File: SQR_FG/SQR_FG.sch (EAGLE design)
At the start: 24 parts, among them IC1 MEGA328P, IC2 NJM7032, Q1 16MHz, SW1 EC12E_SW

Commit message: SQR_FG Bypass by C
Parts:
- removed C7: (no value), rcl:C-EU025-024X044
- removed R4, R5: (no value), rcl:R-EU_0207/7
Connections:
- removed net N$14: C6.2, IC2A.+IN, R4.2
- removed net N$4: C7.1, R4.1, R5.2
- net N$15: now also C6.2, IC2A.+IN; no longer R5.1
- net N$16: no longer C7.2
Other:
- moved on the sheet: C5, C6, IC2A, JP2, R6
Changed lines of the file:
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@@
 <part name="JP2" library="pinhead" deviceset="PINHD-1X2" device=""/>
 <part name="R3" library="rcl" deviceset="R-EU_" device="0207/7" value="33k"/>
-<part name="R4" library="rcl" deviceset="R-EU_" device="0207/7"/>
-<part name="R5" library="rcl" deviceset="R-EU_" device="0207/7"/>
 <part name="C6" library="rcl" deviceset="C-EU" device="025-024X044"/>
-<part name="C7" library="rcl" deviceset="C-EU" device="025-024X044"/>
 <part name="GND6" library="supply1" deviceset="GND" device=""/>
 </parts>
@@
 <instance part="SW1" gate="G$2" x="132.08" y="73.66"/>
 <instance part="GND4" gate="1" x="139.7" y="63.5"/>
-<instance part="P+3" gate="1" x="238.76" y="114.3"/>
-<instance part="GND7" gate="1" x="238.76" y="83.82"/>
-<instance part="IC2" gate="A" x="238.76" y="93.98"/>
+<instance part="P+3" gate="1" x="220.98" y="114.3"/>
+<instance part="GND7" gate="1" x="220.98" y="83.82"/>
+<instance part="IC2" gate="A" x="220.98" y="93.98"/>
 <instance part="IC2" gate="B" x="162.56" y="27.94"/>
-<instance part="IC2" gate="P" x="238.76" y="93.98"/>
-<instance part="R6" gate="G$1" x="259.08" y="93.98"/>
+<instance part="IC2" gate="P" x="220.98" y="93.98"/>
+<instance part="R6" gate="G$1" x="241.3" y="93.98"/>
 <instance part="R7" gate="G$1" x="139.7" y="38.1" rot="R90"/>
 <instance part="R8" gate="G$1" x="139.7" y="22.86" rot="R90"/>
@@
 <instance part="T2" gate="A" x="165.1" y="78.74"/>
 <instance part="GND10" gate="1" x="165.1" y="71.12"/>
-<instance part="C5" gate="G$1" x="243.84" y="104.14" rot="R90"/>
-<instance part="GND5" gate="1" x="254" y="104.14" rot="R90"/>
-<instance part="JP2" gate="G$1" x="274.32" y="91.44"/>
+<instance part="C5" gate="G$1" x="226.06" y="104.14" rot="R90"/>
+<instance part="GND5" gate="1" x="236.22" y="104.14" rot="R90"/>
+<instance part="JP2" gate="G$1" x="256.54" y="91.44"/>
 <instance part="R3" gate="G$1" x="182.88" y="109.22" rot="R90"/>
-<instance part="R4" gate="G$1" x="215.9" y="96.52"/>
-<instance part="R5" gate="G$1" x="200.66" y="96.52"/>
-<instance part="C6" gate="G$1" x="226.06" y="104.14"/>
-<instance part="C7" gate="G$1" x="218.44" y="76.2" rot="R90"/>
-<instance part="GND6" gate="1" x="215.9" y="106.68"/>
+<instance part="C6" gate="G$1" x="208.28" y="104.14"/>
+<instance part="GND6" gate="1" x="198.12" y="106.68"/>
 </instances>
 <busses>
@@
 <pinref part="C5" gate="G$1" pin="2"/>
 <pinref part="GND5" gate="1" pin="GND"/>
-<wire x1="251.46" y1="104.14" x2="248.92" y2="104.14" width="0.1524" layer="91"/>
+<wire x1="233.68" y1="104.14" x2="231.14" y2="104.14" width="0.1524" layer="91"/>
 </segment>
 <segment>
 <pinref part="C6" gate="G$1" pin="1"/>
-<wire x1="226.06" y1="106.68" x2="226.06" y2="111.76" width="0.1524" layer="91"/>
-<wire x1="226.06" y1="111.76" x2="215.9" y2="111.76" width="0.1524" layer="91"/>
+<wire x1="208.28" y1="106.68" x2="208.28" y2="111.76" width="0.1524" layer="91"/>
+<wire x1="208.28" y1="111.76" x2="198.12" y2="111.76" width="0.1524" layer="91"/>
 <pinref part="GND6" gate="1" pin="GND"/>
-<wire x1="215.9" y1="111.76" x2="215.9" y2="109.22" width="0.1524" layer="91"/>
+<wire x1="198.12" y1="111.76" x2="198.12" y2="109.22" width="0.1524" layer="91"/>
 </segment>
 </net>
@@
 <segment>
 <pinref part="IC2" gate="P" pin="V+"/>
-<wire x1="238.76" y1="101.6" x2="238.76" y2="104.14" width="0.1524" layer="91"/>
+<wire x1="220.98" y1="101.6" x2="220.98" y2="104.14" width="0.1524" layer="91"/>
 <pinref part="P+3" gate="1" pin="+5V"/>
 <pinref part="C5" gate="G$1" pin="1"/>
-<wire x1="238.76" y1="104.14" x2="238.76" y2="111.76" width="0.1524" layer="91"/>
-<wire x1="241.3" y1="104.14" x2="238.76" y2="104.14" width="0.1524" layer="91"/>
-<junction x="238.76" y="104.14"/>
+<wire x1="220.98" y1="104.14" x2="220.98" y2="111.76" width="0.1524" layer="91"/>
+<wire x1="223.52" y1="104.14" x2="220.98" y2="104.14" width="0.1524" layer="91"/>
+<junction x="220.98" y="104.14"/>
 </segment>
 </net>
@@
 <net name="N$16" class="0">
 <segment>
-<wire x1="231.14" y1="91.44" x2="228.6" y2="91.44" width="0.1524" layer="91"/>
-<wire x1="228.6" y1="91.44" x2="228.6" y2="76.2" width="0.1524" layer="91"/>
-<wire x1="228.6" y1="76.2" x2="251.46" y2="76.2" width="0.1524" layer="91"/>
-<wire x1="251.46" y1="76.2" x2="251.46" y2="93.98" width="0.1524" layer="91"/>
-<wire x1="251.46" y1="93.98" x2="246.38" y2="93.98" width="0.1524" layer="91"/>
+<wire x1="213.36" y1="91.44" x2="208.28" y2="91.44" width="0.1524" layer="91"/>
+<wire x1="208.28" y1="91.44" x2="208.28" y2="76.2" width="0.1524" layer="91"/>
+<wire x1="208.28" y1="76.2" x2="233.68" y2="76.2" width="0.1524" layer="91"/>
+<wire x1="233.68" y1="76.2" x2="233.68" y2="93.98" width="0.1524" layer="91"/>
+<wire x1="233.68" y1="93.98" x2="228.6" y2="93.98" width="0.1524" layer="91"/>
 <pinref part="IC2" gate="A" pin="-IN"/>
 <pinref part="IC2" gate="A" pin="OUT"/>
 <pinref part="R6" gate="G$1" pin="1"/>
-<wire x1="254" y1="93.98" x2="251.46" y2="93.98" width="0.1524" layer="91"/>
-<junction x="251.46" y="93.98"/>
-<pinref part="C7" gate="G$1" pin="2"/>
-<wire x1="223.52" y1="76.2" x2="228.6" y2="76.2" width="0.1524" layer="91"/>
-<junction x="228.6" y="76.2"/>
+<wire x1="236.22" y1="93.98" x2="233.68" y2="93.98" width="0.1524" layer="91"/>
+<junction x="233.68" y="93.98"/>
 </segment>
 </net>
@@
 <segment>
 <pinref part="R6" gate="G$1" pin="2"/>
-<wire x1="264.16" y1="93.98" x2="271.78" y2="93.98" width="0.1524" layer="91"/>
+<wire x1="246.38" y1="93.98" x2="254" y2="93.98" width="0.1524" layer="91"/>
 <pinref part="JP2" gate="G$1" pin="1"/>
 </segment>
@@
 <wire x1="182.88" y1="86.36" x2="198.12" y2="86.36" width="0.1524" layer="91"/>
 <wire x1="198.12" y1="86.36" x2="198.12" y2="68.58" width="0.1524" layer="91"/>
-<wire x1="198.12" y1="68.58" x2="269.24" y2="68.58" width="0.1524" layer="91"/>
-<wire x1="269.24" y1="68.58" x2="269.24" y2="91.44" width="0.1524" layer="91"/>
+<wire x1="198.12" y1="68.58" x2="251.46" y2="68.58" width="0.1524" layer="91"/>
+<wire x1="251.46" y1="68.58" x2="251.46" y2="91.44" width="0.1524" layer="91"/>
 <pinref part="JP2" gate="G$1" pin="2"/>
-<wire x1="271.78" y1="91.44" x2="269.24" y2="91.44" width="0.1524" layer="91"/>
+<wire x1="254" y1="91.44" x2="251.46" y2="91.44" width="0.1524" layer="91"/>
 </segment>
 </net>
@@
 </segment>
 </net>
-<net name="N$4" class="0">
-<segment>
-<pinref part="R5" gate="G$1" pin="2"/>
-<pinref part="R4" gate="G$1" pin="1"/>
-<wire x1="205.74" y1="96.52" x2="208.28" y2="96.52" width="0.1524" layer="91"/>
-<wire x1="208.28" y1="96.52" x2="210.82" y2="96.52" width="0.1524" layer="91"/>
-<wire x1="218.44" y1="76.2" x2="215.9" y2="76.2" width="0.1524" layer="91"/>
-<wire x1="215.9" y1="76.2" x2="208.28" y2="76.2" width="0.1524" layer="91"/>
-<wire x1="208.28" y1="76.2" x2="208.28" y2="96.52" width="0.1524" layer="91"/>
+<net name="N$15" class="0">
+<segment>
+<wire x1="187.96" y1="96.52" x2="208.28" y2="96.52" width="0.1524" layer="91"/>
+<pinref part="IC2" gate="A" pin="+IN"/>
+<pinref part="C6" gate="G$1" pin="2"/>
+<wire x1="208.28" y1="96.52" x2="213.36" y2="96.52" width="0.1524" layer="91"/>
+<wire x1="208.28" y1="99.06" x2="208.28" y2="96.52" width="0.1524" layer="91"/>
 <junction x="208.28" y="96.52"/>
-<pinref part="C7" gate="G$1" pin="1"/>
-<junction x="215.9" y="76.2"/>
-</segment>
-</net>
-<net name="N$14" class="0">
-<segment>
-<pinref part="R4" gate="G$1" pin="2"/>
-<pinref part="IC2" gate="A" pin="+IN"/>
-<wire x1="220.98" y1="96.52" x2="226.06" y2="96.52" width="0.1524" layer="91"/>
-<pinref part="C6" gate="G$1" pin="2"/>
-<wire x1="226.06" y1="96.52" x2="231.14" y2="96.52" width="0.1524" layer="91"/>
-<wire x1="226.06" y1="99.06" x2="226.06" y2="96.52" width="0.1524" layer="91"/>
-<junction x="226.06" y="96.52"/>
-</segment>
-</net>
-<net name="N$15" class="0">
-<segment>
-<pinref part="R5" gate="G$1" pin="1"/>
-<wire x1="195.58" y1="96.52" x2="187.96" y2="96.52" width="0.1524" layer="91"/>
-</segment>
-</net>
+</segment>
+</net>

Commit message: SQR_FG.sch changed
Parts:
- added C7: (no value), rcl:CPOL-EUE2.5-5
- added R4: 22k, rcl:R-EU_0207/7
- added R5: 12k, rcl:R-EU_0207/7
- C3: value 0.1uF -> (none); device rcl:C-EU025-024X044 -> rcl:CPOL-EUE2.5-5
- JP2: value (none) -> OUT
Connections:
- net N$10 renamed RE_SW
- net N$12 renamed SW_GND
- net N$13 renamed SW_VGND
- net N$5 renamed RE_A
- net N$7 renamed RE_B
- new net AGND: C5.2, C6.1, C7.-, IC2P.V-, R8.1, T2.S
- new net N$4: IC1.PD7(AIN1), R4.1
- net +5V: now also C3.+; no longer C3.1
- net GND: now also R5.2; no longer C3.2, C5.2, C6.1, IC2P.V-, R8.1, T2.S
- net N$17: now also C3.-, C7.+
- net RST: now also R4.2, R5.1; no longer IC1.PD7(AIN1)
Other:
- moved on the sheet: JP1, R3, R7, R8

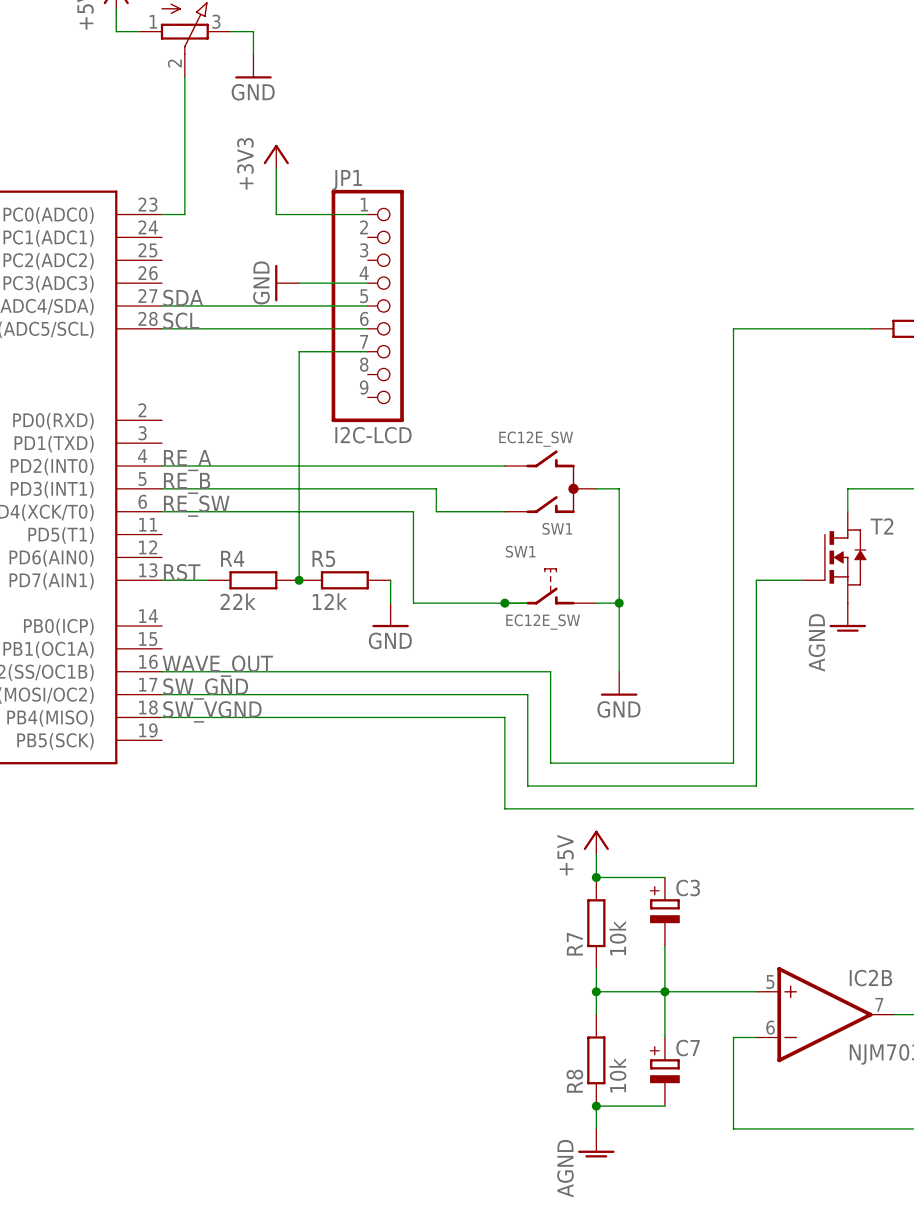
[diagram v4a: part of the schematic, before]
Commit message: SQR_FG Schematic Updated
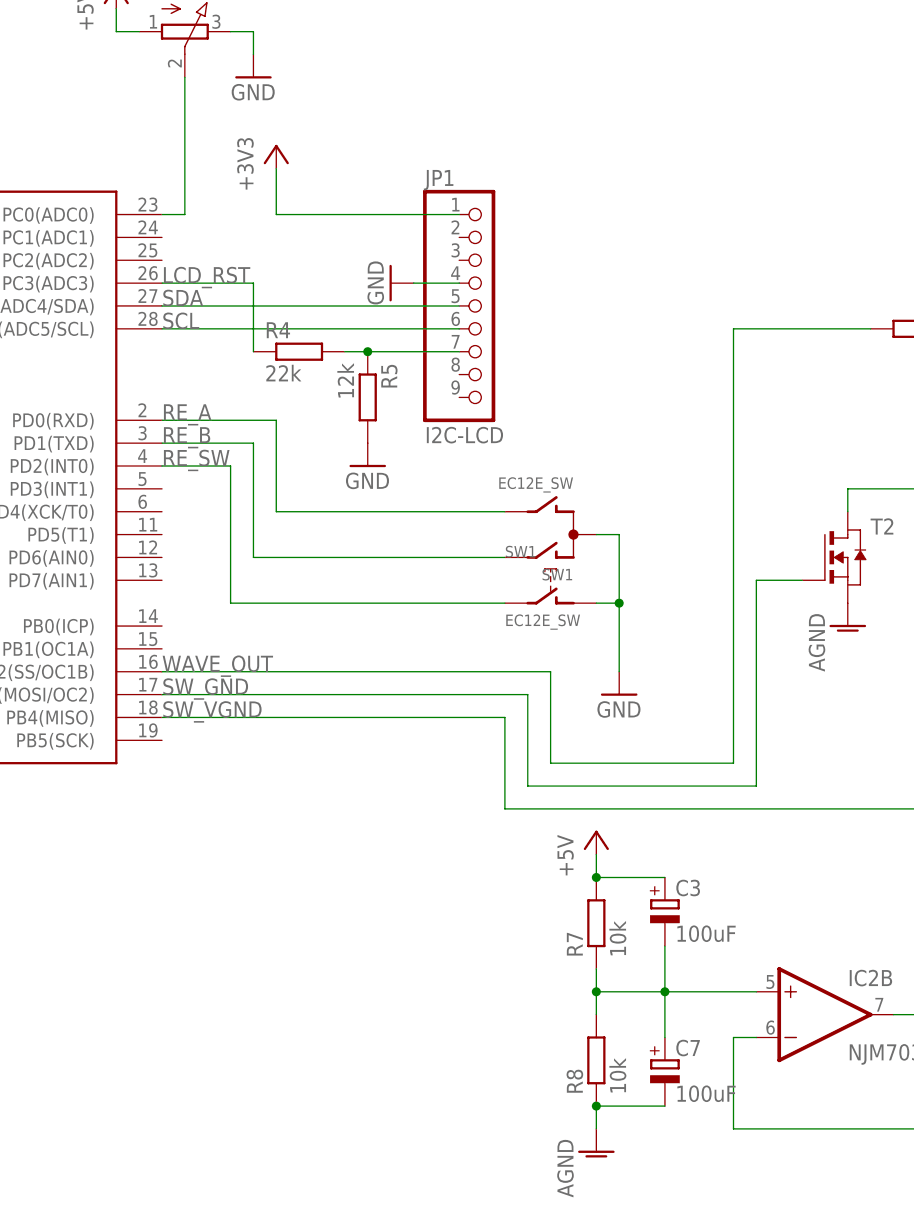
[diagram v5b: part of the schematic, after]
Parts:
- C3, C7: value (none) -> 100uF
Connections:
- removed net N$4: IC1.PD7(AIN1), R4.1
- new net LCD_RST: IC1.PC3(ADC3), R4.1
- net RE_A: now also IC1.PD0(RXD); no longer IC1.PD2(INT0)
- net RE_B: now also IC1.PD1(TXD); no longer IC1.PD3(INT1)
- net RE_SW: now also IC1.PD2(INT0); no longer IC1.PD4(XCK/T0)
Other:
- moved on the sheet: JP1, R4, R5, SW1
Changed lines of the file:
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@@
 <setting verticaltext="up"/>
 </settings>
-<grid distance="0.1" unitdist="inch" unit="inch" style="dots" multiple="1" display="yes" altdistance="0.01" altunitdist="inch" altunit="inch"/>
+<grid distance="0.1" unitdist="inch" unit="inch" style="lines" multiple="1" display="no" altdistance="0.01" altunitdist="inch" altunit="inch"/>
 <layers>
 <layer number="1" name="Top" color="4" fill="1" visible="no" active="no"/>
@@
 <part name="R5" library="rcl" deviceset="R-EU_" device="0207/7" value="12k"/>
 <part name="GND5" library="supply1" deviceset="GND" device=""/>
-<part name="C3" library="rcl" deviceset="CPOL-EU" device="E2.5-5"/>
-<part name="C7" library="rcl" deviceset="CPOL-EU" device="E2.5-5"/>
+<part name="C3" library="rcl" deviceset="CPOL-EU" device="E2.5-5" value="100uF"/>
+<part name="C7" library="rcl" deviceset="CPOL-EU" device="E2.5-5" value="100uF"/>
 </parts>
 <sheets>
 <sheet>
 <plain>
-<wire x1="121.92" y1="96.52" x2="121.92" y2="68.58" width="0" layer="100" style="shortdash"/>
+<wire x1="121.92" y1="88.9" x2="121.92" y2="68.58" width="0" layer="100" style="shortdash"/>
 <wire x1="121.92" y1="68.58" x2="142.24" y2="68.58" width="0" layer="100" style="shortdash"/>
-<wire x1="142.24" y1="68.58" x2="142.24" y2="96.52" width="0" layer="100" style="shortdash"/>
-<wire x1="142.24" y1="96.52" x2="121.92" y2="96.52" width="0" layer="100" style="shortdash"/>
-<text x="121.92" y="99.06" size="1.778" layer="100">Rotary Encoder</text>
+<wire x1="142.24" y1="68.58" x2="142.24" y2="88.9" width="0" layer="100" style="shortdash"/>
+<wire x1="142.24" y1="88.9" x2="121.92" y2="88.9" width="0" layer="100" style="shortdash"/>
+<text x="132.08" y="91.44" size="1.778" layer="100">Rotary Encoder</text>
 </plain>
 <instances>
@@
 <instance part="R1" gate="G$1" x="33.02" y="116.84"/>
 <instance part="P+1" gate="1" x="5.08" y="124.46"/>
-<instance part="JP1" gate="A" x="114.3" y="106.68"/>
+<instance part="JP1" gate="A" x="124.46" y="106.68"/>
 <instance part="+3V1" gate="G$1" x="101.6" y="124.46"/>
-<instance part="GND2" gate="1" x="101.6" y="109.22" rot="R270"/>
+<instance part="GND2" gate="1" x="114.3" y="109.22" rot="R270"/>
 <instance part="R2" gate="G$1" x="91.44" y="137.16" rot="R270"/>
 <instance part="P+2" gate="1" x="83.82" y="142.24"/>
 <instance part="GND3" gate="1" x="99.06" y="132.08"/>
-<instance part="SW1" gate="G$1" x="134.62" y="86.36" rot="R90"/>
+<instance part="SW1" gate="G$1" x="134.62" y="81.28" rot="R90"/>
 <instance part="SW1" gate="G$2" x="132.08" y="73.66"/>
 <instance part="GND4" gate="1" x="139.7" y="63.5"/>
@@
 <instance part="AGND4" gate="VR1" x="236.22" y="104.14" rot="R90"/>
 <instance part="AGND5" gate="VR1" x="137.16" y="12.7"/>
-<instance part="R4" gate="G$1" x="99.06" y="76.2"/>
-<instance part="R5" gate="G$1" x="109.22" y="76.2"/>
-<instance part="GND5" gate="1" x="114.3" y="71.12"/>
+<instance part="R4" gate="G$1" x="104.14" y="101.6"/>
+<instance part="R5" gate="G$1" x="111.76" y="96.52" rot="R270"/>
+<instance part="GND5" gate="1" x="111.76" y="88.9"/>
 <instance part="C3" gate="G$1" x="144.78" y="40.64"/>
 <instance part="C7" gate="G$1" x="144.78" y="22.86"/>
@@
 <pinref part="GND2" gate="1" pin="GND"/>
 <pinref part="JP1" gate="A" pin="4"/>
-<wire x1="104.14" y1="109.22" x2="111.76" y2="109.22" width="0.1524" layer="91"/>
+<wire x1="116.84" y1="109.22" x2="121.92" y2="109.22" width="0.1524" layer="91"/>
 </segment>
 <segment>
@@
 <segment>
 <pinref part="SW1" gate="G$1" pin="C"/>
-<wire x1="137.16" y1="86.36" x2="139.7" y2="86.36" width="0.1524" layer="91"/>
+<wire x1="137.16" y1="81.28" x2="139.7" y2="81.28" width="0.1524" layer="91"/>
 <pinref part="GND4" gate="1" pin="GND"/>
-<wire x1="139.7" y1="86.36" x2="139.7" y2="73.66" width="0.1524" layer="91"/>
+<wire x1="139.7" y1="81.28" x2="139.7" y2="73.66" width="0.1524" layer="91"/>
 <pinref part="SW1" gate="G$2" pin="1"/>
 <wire x1="139.7" y1="73.66" x2="139.7" y2="66.04" width="0.1524" layer="91"/>
@@
 <pinref part="GND5" gate="1" pin="GND"/>
 <pinref part="R5" gate="G$1" pin="2"/>
-<wire x1="114.3" y1="73.66" x2="114.3" y2="76.2" width="0.1524" layer="91"/>
 </segment>
 </net>
@@
 <pinref part="JP1" gate="A" pin="5"/>
 <label x="88.9" y="106.68" size="1.778" layer="95"/>
-<wire x1="88.9" y1="106.68" x2="111.76" y2="106.68" width="0.1524" layer="91"/>
+<wire x1="88.9" y1="106.68" x2="121.92" y2="106.68" width="0.1524" layer="91"/>
 </segment>
 </net>
@@
 <pinref part="IC1" gate="G$1" pin="PC5(ADC5/SCL)"/>
 <pinref part="JP1" gate="A" pin="6"/>
-<wire x1="88.9" y1="104.14" x2="111.76" y2="104.14" width="0.1524" layer="91"/>
+<wire x1="88.9" y1="104.14" x2="121.92" y2="104.14" width="0.1524" layer="91"/>
 <label x="88.9" y="104.14" size="1.778" layer="95"/>
 </segment>
@@
 <segment>
 <pinref part="JP1" gate="A" pin="1"/>
-<wire x1="111.76" y1="116.84" x2="101.6" y2="116.84" width="0.1524" layer="91"/>
+<wire x1="121.92" y1="116.84" x2="101.6" y2="116.84" width="0.1524" layer="91"/>
 <wire x1="101.6" y1="116.84" x2="101.6" y2="121.92" width="0.1524" layer="91"/>
 <pinref part="+3V1" gate="G$1" pin="+3V3"/>
@@
 <segment>
 <pinref part="JP1" gate="A" pin="7"/>
-<wire x1="111.76" y1="101.6" x2="104.14" y2="101.6" width="0.1524" layer="91"/>
-<wire x1="104.14" y1="76.2" x2="104.14" y2="101.6" width="0.1524" layer="91"/>
-<label x="88.9" y="76.2" size="1.778" layer="95"/>
+<wire x1="121.92" y1="101.6" x2="111.76" y2="101.6" width="0.1524" layer="91"/>
 <pinref part="R4" gate="G$1" pin="2"/>
 <pinref part="R5" gate="G$1" pin="1"/>
-<junction x="104.14" y="76.2"/>
+<junction x="111.76" y="101.6"/>
+<wire x1="111.76" y1="101.6" x2="109.22" y2="101.6" width="0.1524" layer="91"/>
 </segment>
 </net>
@@
 </segment>
 </net>
-<net name="RE_A" class="0">
-<segment>
+<net name="RE_B" class="0">
+<segment>
+<pinref part="SW1" gate="G$1" pin="A"/>
+<wire x1="127" y1="78.74" x2="99.06" y2="78.74" width="0.1524" layer="91"/>
+<wire x1="99.06" y1="78.74" x2="99.06" y2="91.44" width="0.1524" layer="91"/>
+<pinref part="IC1" gate="G$1" pin="PD1(TXD)"/>
+<wire x1="99.06" y1="91.44" x2="88.9" y2="91.44" width="0.1524" layer="91"/>
+<label x="88.9" y="91.44" size="1.778" layer="95"/>
+</segment>
+</net>
+<net name="RE_SW" class="0">
+<segment>
+<pinref part="SW1" gate="G$2" pin="2"/>
+<wire x1="127" y1="73.66" x2="96.52" y2="73.66" width="0.1524" layer="91"/>
+<wire x1="96.52" y1="73.66" x2="96.52" y2="88.9" width="0.1524" layer="91"/>
 <pinref part="IC1" gate="G$1" pin="PD2(INT0)"/>
-<pinref part="SW1" gate="G$1" pin="B"/>
-<wire x1="88.9" y1="88.9" x2="127" y2="88.9" width="0.1524" layer="91"/>
+<wire x1="96.52" y1="88.9" x2="88.9" y2="88.9" width="0.1524" layer="91"/>
 <label x="88.9" y="88.9" size="1.778" layer="95"/>
-</segment>
-</net>
-<net name="RE_B" class="0">
-<segment>
-<pinref part="IC1" gate="G$1" pin="PD3(INT1)"/>
-<wire x1="88.9" y1="86.36" x2="119.38" y2="86.36" width="0.1524" layer="91"/>
-<wire x1="119.38" y1="86.36" x2="119.38" y2="83.82" width="0.1524" layer="91"/>
-<pinref part="SW1" gate="G$1" pin="A"/>
-<wire x1="119.38" y1="83.82" x2="127" y2="83.82" width="0.1524" layer="91"/>
-<label x="88.9" y="86.36" size="1.778" layer="95"/>
-</segment>
-</net>
-<net name="RE_SW" class="0">
-<segment>
-<pinref part="IC1" gate="G$1" pin="PD4(XCK/T0)"/>
-<wire x1="88.9" y1="83.82" x2="116.84" y2="83.82" width="0.1524" layer="91"/>
-<wire x1="116.84" y1="83.82" x2="116.84" y2="73.66" width="0.1524" layer="91"/>
-<wire x1="116.84" y1="73.66" x2="127" y2="73.66" width="0.1524" layer="91"/>
-<pinref part="SW1" gate="G$2" pin="2"/>
-<wire x1="127" y1="73.66" x2="129.54" y2="73.66" width="0.1524" layer="91"/>
-<junction x="127" y="73.66"/>
-<label x="88.9" y="83.82" size="1.778" layer="95"/>
 </segment>
 </net>
@@
 </segment>
 </net>
-<net name="N$4" class="0">
-<segment>
-<pinref part="R4" gate="G$1" pin="1"/>
-<pinref part="IC1" gate="G$1" pin="PD7(AIN1)"/>
-<wire x1="93.98" y1="76.2" x2="88.9" y2="76.2" width="0.1524" layer="91"/>
-</segment>
-</net>
 <net name="N$8" class="0">
 <segment>
@@
 </segment>
 </net>
+<net name="RE_A" class="0">
+<segment>
+<pinref part="SW1" gate="G$1" pin="B"/>
+<wire x1="127" y1="83.82" x2="101.6" y2="83.82" width="0.1524" layer="91"/>
+<wire x1="101.6" y1="83.82" x2="101.6" y2="93.98" width="0.1524" layer="91"/>
+<pinref part="IC1" gate="G$1" pin="PD0(RXD)"/>
+<wire x1="101.6" y1="93.98" x2="88.9" y2="93.98" width="0.1524" layer="91"/>
+<label x="88.9" y="93.98" size="1.778" layer="95"/>
+</segment>
+</net>
+<net name="LCD_RST" class="0">
+<segment>
+<pinref part="IC1" gate="G$1" pin="PC3(ADC3)"/>
+<wire x1="88.9" y1="109.22" x2="99.06" y2="109.22" width="0.1524" layer="91"/>
+<pinref part="R4" gate="G$1" pin="1"/>
+<wire x1="99.06" y1="109.22" x2="99.06" y2="101.6" width="0.1524" layer="91"/>
+<label x="88.9" y="109.22" size="1.778" layer="95"/>
+</segment>
+</net>
